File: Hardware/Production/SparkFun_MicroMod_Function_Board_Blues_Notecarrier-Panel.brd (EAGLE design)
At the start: 133.6 x 79.2 mm, 267 parts, among them J10 MICROMOD_FUNCTION_STANDARD, J14 NOTECARD, J15 MICROMOD_FUNCTION_STANDARD, J2 MICROMOD_FUNCTION_STANDARD, J6 NOTECARD, J9 NOTECARD, Q1 220mA/50V/3.5Ω, Q10 220mA/50V/3.5Ω, Q11 20V/4.2A/52mΩ/1.4W, Q12 20V/4.2A/52mΩ/1.4W, Q2 20V/4.2A/52mΩ/1.4W, Q3 220mA/50V/3.5Ω, Q4 20V/4.2A/52mΩ/1.4W, Q5 220mA/50V/3.5Ω, Q6 220mA/50V/3.5Ω, Q7 20V/4.2A/52mΩ/1.4W, Q8 20V/4.2A/52mΩ/1.4W, Q9 220mA/50V/3.5Ω, U1 EEPROM, U2 TCR2EF33, U3 EEPROM, U4 TCR2EF33, U5 EEPROM, U6 TCR2EF33

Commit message: Added v02 panel/gerbers.
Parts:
- removed ANT_PWR2, WP2: JUMPER-SMT_2_NO_SILK, SparkFun-Jumpers:SMT-JUMPER_2_NO_SILK
- removed AUX_EN_LED2, PWR_LED2, SHLD2, VIO_LED2: JUMPER-SMT_2_NC_TRACE_SILK, SparkFun-Jumpers:SMT-JUMPER_2_NC_TRACE_SILK
- removed C21, C23: 0.1uF, SparkFun-Capacitors:0402-TIGHT
- removed C22: 10uF, SparkFun-Capacitors:0805
- removed C24: 1.0uF, SparkFun-Capacitors:0402-TIGHT
- removed D21: RED, SparkFun-LED:LED-0603
- removed D22: BLUE, SparkFun-LED:LED-0603
- removed D23, D24: 0.5A/40V/420mV, SparkFun-DiscreteSemi:SOD-323
- removed FD10, FD11, FD12, FD9: FIDUCIALUFIDUCIAL, SparkFun-Aesthetics:FIDUCIAL-MICRO
- removed H3: STAND-OFF-REFLOW-M2.5_2.5MM_TALL, SparkFun-Hardware:STAND-OFF-REFLOW-M2.5
- removed J11: (no value), SparkFun-Connectors:USB-C-16P-2LAYER-PADS
- removed J12: (no value), SparkFun-Connectors:NANO_SIM_MOLEX_104224-0820
- removed J13: (no value), SparkFun-Connectors:1X06_NO_SILK
- removed J14: NOTECARD, SparkFun_MicroMod_Function_Board_Blues_Notecarrier:M.2-CONNECTOR-E
- removed J15: MICROMOD_FUNCTION_STANDARD, SparkFun-MicroMod:M.2-CARD-E-22_FUNCTION_STANDARD
- removed LOGO5: OSHW-LOGOMINI, SparkFun-Aesthetics:OSHW-LOGO-MINI
- removed LOGO6: SFE_LOGO_NAME_FLAME.1_INCH, SparkFun-Aesthetics:SFE_LOGO_NAME_FLAME_.1
- removed MEAS2: JUMPER-COMBO_2_NC_TRACE, SparkFun-Jumpers:COMBO-JUMPER_2_NC_TRACE
- removed R35, R36, R37, R44, R45: 10k, SparkFun-Resistors:0402-TIGHT
- removed R38, R39: 5.1k, SparkFun-Resistors:0402-TIGHT
- removed R40, R41: 1k, SparkFun-Resistors:0402-TIGHT
- removed R42: 4.7k, SparkFun-Resistors:0402-TIGHT
- removed R43: 2.2M, SparkFun-Resistors:0402-TIGHT
- removed R46, R47: 100, SparkFun-Resistors:0402-TIGHT
- removed R48: 1, SparkFun-Resistors:0603
- removed S3: MOMENTARY-SWITCH-SPST-SMD-4.6X2.8MM, SparkFun-Switches:TACTILE_SWITCH_SMD_4.6X2.8MM
- removed U$55, U$84: (no value), SparkFun-MicroMod:MICROMOD_LOGO_.3
- removed U$56, U$85: (no value), SparkFun-MicroMod:MICROMOD_MI_LOGO_.35
- removed U$57, U$86: (no value), output:#_AUX1#MCU_#DFU_STAT##0
- removed U$58, U$87: (no value), output:#AUX_EN_#0
- removed U$59: (no value), output:AEN1
- removed U$60: (no value), output:VIN3
- removed U$61: (no value), output:VIO4
- removed U$62: (no value), output:##RESET##9
- removed U$63: (no value), SparkFun-Aesthetics:SFE_LOGO_FLAME_STOP_.1
- removed U$64: (no value), output:#_GND_#0
- removed U$65: (no value), output:#_AUX4#MCU_#RST##0
- removed U$66: (no value), output:#_AUX3#MCU_#BOOT##0
- removed U$67: (no value), output:#_AUX2#0
- removed U$68: (no value), output:#_AUX_EN#0
- removed U$69: (no value), SparkFun-Aesthetics:SFE_LOGO_NAME_FLAME_.1
- removed U$70: (no value), output:BLUES_WIRELESS_NOTECARRIER1
- removed U$71: (no value), output:#_WP#2
- removed U$72, U$73: (no value), output:#MEAS#4
- removed U$74: (no value), output:#_ANT_PWR#5
- removed U$75: (no value), output:#PWR_LED_#17
- removed U$76: (no value), output:#AUX_EN_LED_#20
- removed U$77: (no value), output:#VIO_LED_#21
- removed U$78: (no value), output:#_SHLD#23
- removed U$79: (no value), output:#_GND_#24
- removed U$80: (no value), output:#AUX4#MCU_#RST##0
- removed U$81: (no value), output:#AUX3#MCU_#BOOT##0
- removed U$82: (no value), output:#AUX2_#0
- removed U$83: (no value), output:#AUX1#MCU_#DFU_STAT##0
- removed U5: EEPROM, SparkFun-IC-Memory:SO08
- removed U6: TCR2EF33, SparkFun_MicroMod_Function_Board_Blues_Notecarrier:SOT23-5
- added RGB, RGB1: JUMPER-SMT_2_NC_TRACE_SILK, SparkFun-Jumpers:SMT-JUMPER_2_NC_TRACE_SILK
- C10, C11: value 100uF -> 0.1uF; device SparkFun-Capacitors:PANASONIC_D -> SparkFun-Capacitors:0402-TIGHT
- C12, C13: value 0.1uF -> 100uF; device SparkFun-Capacitors:0402-TIGHT -> SparkFun-Capacitors:PANASONIC_D
- C14: value 10uF -> 0.1uF; device SparkFun-Capacitors:0805 -> SparkFun-Capacitors:0402-TIGHT
- C16: value 1.0uF -> 10uF; device SparkFun-Capacitors:0402-TIGHT -> SparkFun-Capacitors:0805
- C18, C19: value 100uF -> 1.0uF; device SparkFun-Capacitors:PANASONIC_D -> SparkFun-Capacitors:0402-TIGHT
- C9: value 0.1uF -> 1.0uF
- D10: value 3A/10V/280mV -> WS2812_2020; device SparkFun-DiscreteSemi:SOD-323 -> SparkFun-LED:WS2812-2020
- D11: value 3A/10V/280mV -> PRTR5V0U2F; device SparkFun-DiscreteSemi:SOD-323 -> SparkFun-IC-Power:SOT886
- D12, D13: value RED -> 3A/10V/280mV; device SparkFun-LED:LED-0603 -> SparkFun-DiscreteSemi:SOD-323
- D14: value BLUE -> RED
- D15: value 0.5A/40V/420mV -> RED; device SparkFun-DiscreteSemi:SOD-323 -> SparkFun-LED:LED-0603
- D16: value 0.5A/40V/420mV -> BLUE; device SparkFun-DiscreteSemi:SOD-323 -> SparkFun-LED:LED-0603
- D17: value PRTR5V0U2F -> 0.5A/40V/420mV; device SparkFun-IC-Power:SOT886 -> SparkFun-DiscreteSemi:SOD-323
- D18: value 3A/10V/280mV -> 0.5A/40V/420mV
- D19: value 3A/10V/280mV -> SMBJP6KE6.8A-TP; device SparkFun-DiscreteSemi:SOD-323 -> SparkFun_MicroMod_Function_Board_Blues_Notecarrier:DO-214AA
- D20: value RED -> WS2812_2020; device SparkFun-LED:LED-0603 -> SparkFun-LED:WS2812-2020
- D9: value PRTR5V0U2F -> SMBJP6KE6.8A-TP; device SparkFun-IC-Power:SOT886 -> SparkFun_MicroMod_Function_Board_Blues_Notecarrier:DO-214AA
- J10: value MICROMOD_FUNCTION_STANDARD -> (none); device SparkFun-MicroMod:M.2-CARD-E-22_FUNCTION_STANDARD -> SparkFun-Connectors:1X04_NO_SILK
- J3: device SparkFun-Connectors:USB-C-16P-2LAYER-PADS -> SparkFun-Connectors:1X04_NO_SILK
- J4: device SparkFun-Connectors:1X06_NO_SILK -> SparkFun-Connectors:USB-C-16P-2LAYER-PADS
- J8: value (none) -> NOTECARD; device SparkFun-Connectors:1X06_NO_SILK -> SparkFun_MicroMod_Function_Board_Blues_Notecarrier:M.2-CONNECTOR-E
- J9: value NOTECARD -> MICROMOD_FUNCTION_STANDARD; device SparkFun_MicroMod_Function_Board_Blues_Notecarrier:M.2-CONNECTOR-E -> SparkFun-MicroMod:M.2-CARD-E-22_FUNCTION_STANDARD
- Q10, Q6, Q9: value 220mA/50V/3.5Ω -> 20V/4.2A/52mΩ/1.4W
- Q11, Q7, Q8: value 20V/4.2A/52mΩ/1.4W -> 220mA/50V/3.5Ω
- R17: value 10k -> 100
- R18: value 560Ω -> 10k
- R19: value 10k -> 560Ω
- R22: value 5.1k -> 10k
- R24: value 1k -> 5.1k
- R26: value 4.7k -> 1k
- R27: value 2.2M -> 2.2k
- R28: value 10k -> 2.2M
- R34: value 560Ω -> 100
- R6: value 4.7k -> 2.2k
- U$10: device output:#_AUX3#MCU_#BOOT##0 -> notehub:NOTEHUB_BLUES#SVG7
- U$11: device output:#_AUX2#0 -> output:#_ATXO#0
- U$12: device output:#_AUX1#MCU_#DFU_STAT##0 -> output:#AUX_TX_#0
- U$13: device output:#_AUX_EN#0 -> output:#_AEN#0
- U$14: device SparkFun-Aesthetics:SFE_LOGO_NAME_FLAME_.1 -> SparkFun-Aesthetics:SFE_LOGO_NAME_FLAME_.2
- U$15: device output:BLUES_WIRELESS_NOTECARRIER1 -> output:#AUX_RX_#0
- U$23: device output:AEN1 -> notehub:NOTEHUB_BLUES#SVG5
- U$24: device output:#AUX4#MCU_#RST##0 -> output:#RGB_#0
- U$25: device output:#AUX3#MCU_#BOOT##0 -> output:AEN1
- U$26: device output:#AUX2_#0 -> output:VIN3
- U$27: device output:#AUX1#MCU_#DFU_STAT##0 -> output:VIO4
- U$28: device SparkFun-MicroMod:MICROMOD_LOGO_.3 -> SparkFun-Aesthetics:SFE_LOGO_FLAME_STOP_.1
- U$31: device output:VIN3 -> SparkFun-MicroMod:MICROMOD_LOGO_.5
- U$32: device output:VIO4 -> output:#_GND_#0
- U$33: device output:##RESET##9 -> SparkFun-Aesthetics:SFE_LOGO_NAME_FLAME_.2
- U$34: device SparkFun-Aesthetics:SFE_LOGO_FLAME_STOP_.1 -> output:#_WP#2
- U$35: device output:#_GND_#0 -> output:#MEAS#4
- U$36: device output:#_AUX4#MCU_#RST##0 -> output:#MEAS#4
- U$37: device output:#_AUX3#MCU_#BOOT##0 -> output:#_ANT_PWR#5
- U$38: device output:#_AUX2#0 -> output:#PWR_LED_#17
- U$39: device output:#_AUX_EN#0 -> output:#AUX_EN_LED_#20
- U$40: device SparkFun-Aesthetics:SFE_LOGO_NAME_FLAME_.1 -> output:#VIO_LED_#21
- U$41: device output:BLUES_WIRELESS_NOTECARRIER1 -> output:#_SHLD#23
- U$42: device output:#_WP#2 -> output:#_GND_#24
- U$43: device output:#MEAS#4 -> SparkFun-MicroMod:MICROMOD_MI_LOGO_.35
- U$44: device output:#MEAS#4 -> output:#AUX_EN_#0
- U$45: device output:#_ANT_PWR#5 -> notehub:NOTEHUB_BLUES#SVG5
- U$46: device output:#PWR_LED_#17 -> SparkFun-MicroMod:MICROMOD_LOGO_.5
- U$47: device output:#AUX_EN_LED_#20 -> output:BLUES_WIRELESS_NOTECARRIER0
- U$48: device output:#VIO_LED_#21 -> notehub:NOTEHUB_BLUES#SVG7
- U$49: device output:#_SHLD#23 -> output:#AUX_TX_#0
- U$5: device output:##RESET##9 -> output:#_ARXI#0
- U$50: device output:#_GND_#24 -> output:#AUX_RX_#0
- U$51: device output:#AUX4#MCU_#RST##0 -> output:#_ARXI#0
- U$52: device output:#AUX3#MCU_#BOOT##0 -> output:#_ATXO#0
- U$53: device output:#AUX2_#0 -> output:#_AEN#0
- U$54: device output:#AUX1#MCU_#DFU_STAT##0 -> output:#RGB_#0
- U$9: device output:#_AUX4#MCU_#RST##0 -> output:BLUES_WIRELESS_NOTECARRIER0
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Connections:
- removed net !RESET!: J6.67, S1.3, S1.4
- removed net !RESET!1: J9.67, S2.3, S2.4
- removed net !RESET!2: J14.67, S3.3, S3.4
- removed net 3.3V2: C17.1, C20.1, D20.A, D23.C, D24.C, J14.2, J14.4, R33.1, R44.1, U5.8
- removed net 3V3_IN2: J15.73, Q11.2, R35.1, R36.2
- removed net A6: J15.36, U5.1
- removed net A7: J15.32, U5.3
- removed net A8: J15.34, U5.2
- removed net ATTN2: J14.54, J15.53
- removed net AUX1: J10.57, J8.5, J9.48
- removed net AUX1/MCU_!DFU_STAT!: J2.10, J4.6, J6.46
- removed net AUX1/MCU_!DFU_STAT!1: J10.10, J8.6, J9.46
- removed net AUX1/MCU_!DFU_STAT!2: J13.6, J14.46, J15.10
- removed net AUX2: J2.57, J4.5, J6.48
- removed net AUX3: J13.5, J14.48, J15.57
- removed net AUX3/MCU_!BOOT!: J2.66, J4.4, J6.50
- removed net AUX3/MCU_!BOOT!1: J10.66, J8.4, J9.50
- removed net AUX3/MCU_!BOOT!2: J13.4, J14.50, J15.66
- removed net AUX4/MCU_!RST!: J2.68, J4.3, J6.52
- removed net AUX4/MCU_!RST!1: J10.68, J8.3, J9.52
- removed net AUX4/MCU_!RST!2: J13.3, J14.52, J15.68
- removed net AUX_EN2: D22.A, J13.2, J14.56, J15.55, R44.2
- removed net AUX_RX/MCU_TX2: J14.58, J15.4
- removed net AUX_TX/MCU_RX2: J14.60, J15.6
- removed net EWP2: J15.40, R33.2, U5.7, WP2.2
- removed net GND2: AUX_EN_LED2.1, C17.2, C18.-, C19.-, C20.2, C21.2, C22.2, C23.2, C24.2, D17.2, H3.1, J11.GND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
- removed net N$33 (its old number): Q5.3, R30.1
- removed net N$39 (its old number): Q12.1, R37.1, R47.2
- removed net N$43: D20.C, R40.2
- removed net N$44: D21.C, R41.2
- removed net N$45: PWR_LED2.2, R41.1
- removed net N$46: R40.1, VIO_LED2.2
- removed net N$47: D22.C, R42.2
- removed net N$48: AUX_EN_LED2.2, R42.1
- removed net N$49: R45.1, U6.3
- removed net N$50: C24.1, D23.A, U6.5
- removed net N$51: D24.A, Q11.3
- removed net N$52: Q9.3, R46.1
- removed net N$53: Q10.3, R47.1
- removed net N$54: MEAS2.2, MEAS2.4, R48.1
- removed net NOTECARD_RX2: J14.62, J15.13
- removed net NOTECARD_TX2: J14.64, J15.15
- removed net PWR_EN2: Q10.1, Q9.1, R34.1, R35.2
- removed net SCL2: J14.40, J15.21, U5.6
- removed net SDA2: J14.42, J15.19, U5.5
- removed net SHLD2: J11.SHLD1, J11.SHLD2, J11.SHLD3, J11.SHLD4, SHLD2.2
- removed net SIM_CLK2: J12.S3, J14.14
- removed net SIM_IO2: J12.S6, J14.12
- removed net SIM_RST2: J12.S2, J14.10
- removed net SIM_VCC2: C22.1, J12.S1, J14.8
- removed net USB_IN_N2: D17.3, J11.A7, J11.B7
- removed net USB_IN_P2: D17.1, J11.A6, J11.B6
- removed net USB_N2: D17.4, J14.9
- removed net USB_P2: D17.6, J14.7
- removed net VACT_GPS_IN2: ANT_PWR2.2, J14.22
- removed net VACT_GPS_OUT2: ANT_PWR2.1, J14.20
- removed net VCC2: D19.A, Q12.3
- removed net VCC_IN2: J15.72, J15.74, Q12.2, R37.2
- removed net VIN2: C18.+, C19.+, C21.1, C23.1, D21.A, J14.70, J14.72, J14.74, R43.2, R45.2, R48.2, U6.1
- removed net V_USB2: D17.5, D18.A, J11.VBUS1, J11.VBUS2, J14.13
- new net AUX1/DFU_!ACTIVE!/USR_BTN: C9.1, D9.C, J2.10, J6.46, S1.3, S1.4
- new net AUX1/DFU_!ACTIVE!/USR_BTN1: C19.1, D19.C, J8.46, J9.10, S2.3, S2.4
- new net AUX2/RGB: D10.DI, J2.57, J6.48
- new net AUX2/RGB1: D20.DI, J8.48, J9.57
- new net AUX3/DFU_!BOOT!: J2.66, J6.50
- new net AUX3/DFU_!BOOT!1: J8.50, J9.66
- new net AUX4/DFU_!RST!: J2.68, J6.52
- new net AUX4/DFU_!RST!1: J8.52, J9.68
- new net AUX_PWR: J2.55, Q5.1
- new net AUX_PWR1: J9.55, Q11.1
- new net N$30: R25.1, VIO_LED1.2
- new net N$35: D18.A, Q9.3
- net 3.3V: now also Q6.2, R10.2, RGB.2; no longer R10.1
- net 3.3V1: now also C11.1, C14.1, D14.A, D17.C, D18.C, J8.2, J8.4, Q12.2, R18.1, R33.2, RGB1.2; no longer C12.1, C9.1, D12.A, D15.C, D16.C, J9.2, J9.4, R17.1, R28.1
- net 3V3_IN1: now also J9.73, Q9.2, R20.1, R21.2; no longer J10.73, Q7.2, R19.1, R20.2
- net A3: now also J9.36; no longer J10.36
- net A4: now also J9.32; no longer J10.32
- net A5: now also J9.34; no longer J10.34
- net ATTN1: now also J8.54, J9.53; no longer J10.53, J9.54
- net AUX_EN: now also J3.4, Q6.3; no longer J2.55, J4.2, R10.2
- net AUX_EN1: now also D16.A, J10.4, J8.56, Q12.3; no longer D14.A, J10.55, J8.2, J9.56, R28.2
- net AUX_RX/MCU_TX: now also J2.6, J3.3; no longer J2.4
- net AUX_RX/MCU_TX1: now also J10.3, J8.58, J9.6; no longer J10.4, J9.58
- net AUX_TX/MCU_RX: now also J2.4, J3.2; no longer J2.6
- net AUX_TX/MCU_RX1: now also J10.2, J8.60, J9.4; no longer J10.6, J9.60
- net EWP1: now also J9.40, R18.2; no longer J10.40, R17.2
- net GND: now also C10.2, C9.2, D10.GND, D9.A, J3.1, Q5.2; no longer J4.1
- net GND1: now also C11.2, C12.-, C13.-, C17.2, C18.2, C19.2, C20.2, D11.2, D19.A, D20.GND, J4.GND, J4.GND2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; no longer C10.-, C11.-, C12.2, C13.2, C9.2, D9.2, J10.2, J10.33, J10.39, J10.45, J10.75, J10.8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
- net N$18: now also C10.1, D10.VCC, RGB.1; no longer J10.71, R18.2
- net N$19: now also Q6.1, R10.1, R17.2; no longer Q7.1, R20.1, R30.2
- net N$20: now also Q5.3, R17.1; no longer Q8.1, R21.1, R31.2
- net N$21: now also J9.71, R19.2; no longer J3.B5, R22.2
- net N$22: now also Q9.1, R21.1, R30.2; no longer J3.A5, R23.2
- net N$23: now also Q10.1, R22.1, R31.2; no longer D10.C, D11.C, MEAS1.1, MEAS1.3
- net N$24: now also J4.B5, R23.2; no longer D12.C, R24.2
- net N$25: now also J4.A5, R24.2; no longer D13.C, R25.2
- net N$26: now also D12.C, D13.C, MEAS1.1, MEAS1.3; no longer PWR_LED1.2, R25.1
- net N$27: now also D14.C, R25.2; no longer R24.1, VIO_LED1.2
- net N$28: now also D15.C; no longer D14.C
- net N$29: now also PWR_LED1.2; no longer AUX_EN_LED1.2
- net N$31: now also D16.C, R27.2; no longer C16.1, D15.A, U4.5
- net N$32: now also AUX_EN_LED1.2, R27.1; no longer D16.A, Q7.3
- net N$34: now also C18.1, D17.A, U4.5; no longer Q6.3, R31.1
- net N$36: now also Q7.3, R30.1; no longer J15.71, R34.2
- net N$38: now also Q8.3, R31.1; no longer Q11.1, R36.1, R46.2
- net N$40: now also C20.1, D20.VCC, RGB1.1; no longer J11.B5, R38.2
- net N$41: now also Q12.1, R33.1, R34.2; no longer J11.A5, R39.2
- net N$42: now also Q11.3, R34.1; no longer D18.C, D19.C, MEAS2.1, MEAS2.3
- net NOTECARD_RX1: now also J8.62, J9.13; no longer J10.13, J9.62
- net NOTECARD_TX1: now also J8.64, J9.15; no longer J10.15, J9.64
- net PWR_EN1: now also Q7.1, Q8.1, R19.1, R20.2; no longer Q5.1, Q6.1, R18.1, R19.2
- net SCL1: now also J8.40, J9.21; no longer J10.21, J9.40
- net SDA1: now also J8.42, J9.19; no longer J10.19, J9.42
- net SHLD1: now also J4.SHLD1, J4.SHLD2, J4.SHLD3, J4.SHLD4; no longer J3.SHLD1, J3.SHLD2, J3.SHLD3, J3.SHLD4
- net SIM_CLK1: now also J8.14; no longer J9.14
- net SIM_IO1: now also J8.12; no longer J9.12
- net SIM_RST1: now also J8.10; no longer J9.10
- net SIM_VCC1: now also C16.1, J8.8; no longer C14.1, J9.8
- net USB_IN_N1: now also D11.3, J4.A7, J4.B7; no longer D9.3, J3.A7, J3.B7
- net USB_IN_P1: now also D11.1, J4.A6, J4.B6; no longer D9.1, J3.A6, J3.B6
- net USB_N1: now also D11.4, J8.9; no longer D9.4, J9.9
- net USB_P1: now also D11.6, J8.7; no longer D9.6, J9.7
- net VACT_GPS_IN1: now also J8.22; no longer J9.22
- net VACT_GPS_OUT1: now also J8.20; no longer J9.20
- net VCC1: now also D13.A, Q10.3; no longer D11.A, Q8.3
- net VCC_IN1: now also J9.72, J9.74, Q10.2, R22.2; no longer J10.72, J10.74, Q8.2, R21.2
- net VIN1: now also C12.+, C13.+, C17.1, D15.A, J8.70, J8.72, J8.74, R28.2; no longer C10.+, C11.+, C13.1, D13.A, J9.70, J9.72, J9.74, R27.2
- net V_USB1: now also D11.5, D12.A, J4.VBUS1, J4.VBUS2, J8.13; no longer D10.A, D9.5, J3.VBUS1, J3.VBUS2, J9.13
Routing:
- net AUX_EN2: track 97.9 -> 0.00 mm, vias 7 -> 0
- net VIN2: track 92.7 -> 0.00 mm, vias 3 -> 0
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- added copper zone on layer 1, net AUX1/DFU_!ACTIVE!/USR_BTN
- added copper zone on layer 1, net AUX1/DFU_!ACTIVE!/USR_BTN1
- added copper zone on layer 1, net N$34
- removed copper zone on layer 1, net 3.3V2
- removed copper zone on layer 1, net GND2
- removed copper zone on layer 16, net GND2
- removed copper zone on layer 1, net N$31
- removed copper zone on layer 1, net N$50
- removed copper zone on layer 1, net SHLD2
- removed copper zone on layer 16, net SHLD2
- removed copper zone on layer 1, net SIM_VCC2
- removed copper zone on layer 16, net SIM_VCC2
- removed copper zone on layer 1, net VCC_IN2
- removed copper zone on layer 16, net VCC_IN2
- removed copper zone on layer 1, net VIN2
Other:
- board size 133.6 x 79.2 mm -> 95.6 x 79.2 mm
- board text added: "v02"
- board text removed: "v01"

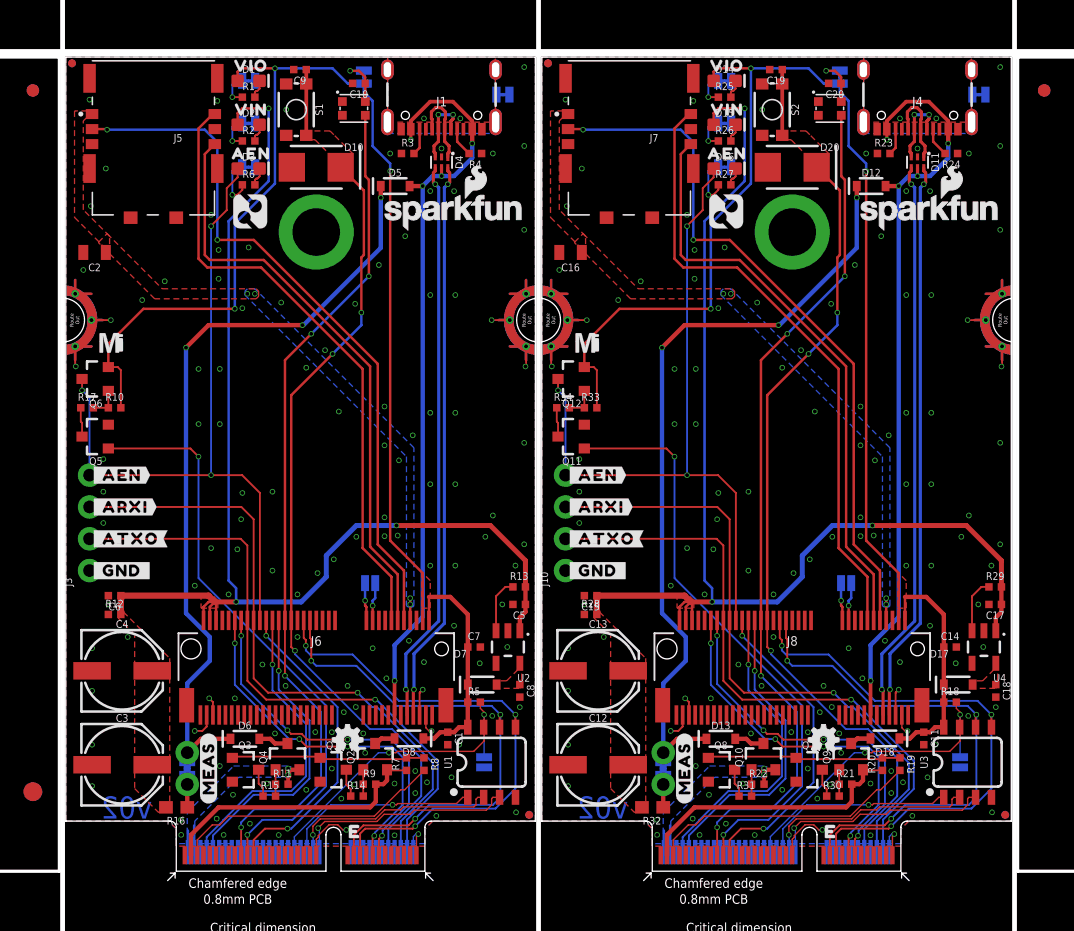
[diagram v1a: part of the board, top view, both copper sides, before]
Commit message: Swap Notecard RX/TX, add missing silk, add diode PROD-ID.
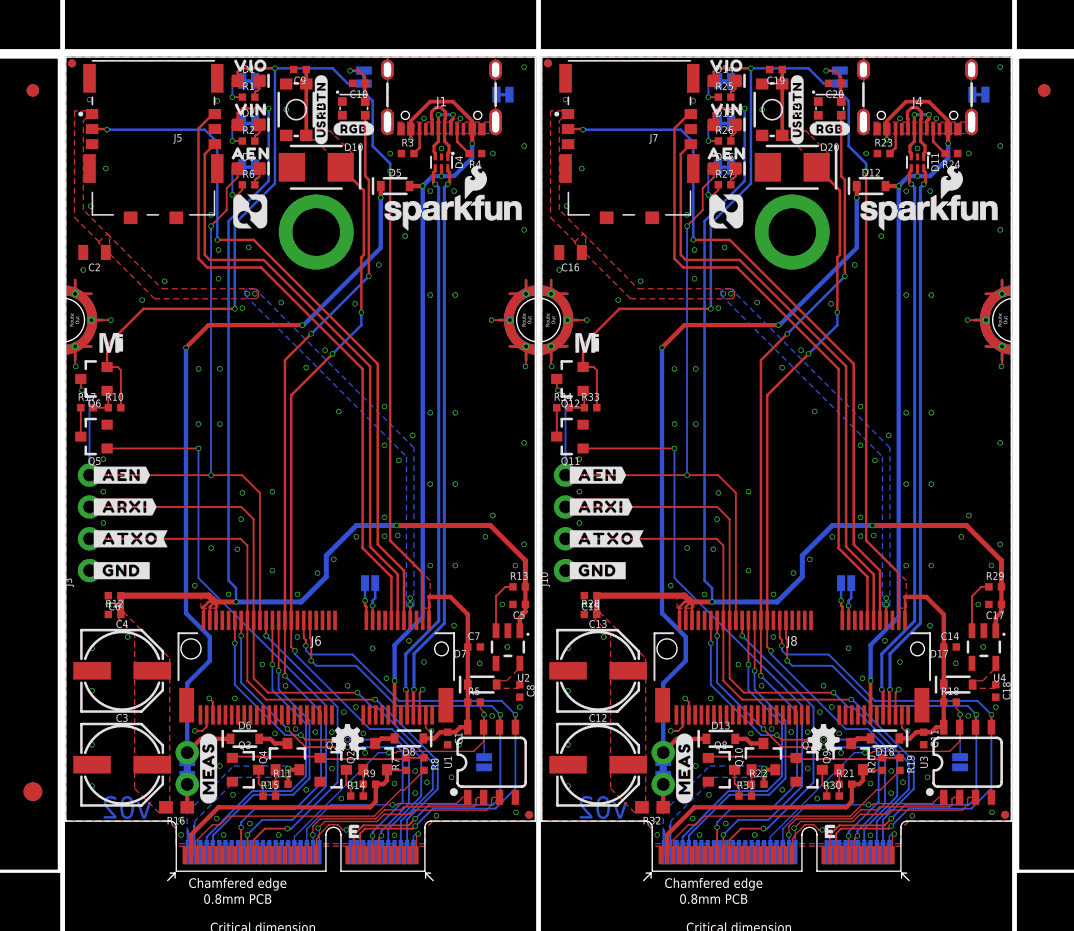
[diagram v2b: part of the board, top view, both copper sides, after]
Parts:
- added U$55: (no value), output:#_AEN#0
- added U$56: (no value), output:#RGB_#0
- added U$57: (no value), output:#USRBTN#0
- added U$58: (no value), output:#RGB#0
- U$25: device output:AEN1 -> output:#USRBTN#0
- U$26: device output:VIN3 -> output:#RGB#0
- U$27: device output:VIO4 -> output:AEN1
- U$28: device SparkFun-Aesthetics:SFE_LOGO_FLAME_STOP_.1 -> output:VIN3
- U$32: device output:#_GND_#0 -> output:VIO4
- U$33: device SparkFun-Aesthetics:SFE_LOGO_NAME_FLAME_.2 -> SparkFun-Aesthetics:SFE_LOGO_FLAME_STOP_.1
- U$34: device output:#_WP#2 -> output:#_GND_#0
- U$35: device output:#MEAS#4 -> SparkFun-Aesthetics:SFE_LOGO_NAME_FLAME_.2
- U$36: device output:#MEAS#4 -> output:#_WP#2
- U$37: device output:#_ANT_PWR#5 -> output:#MEAS#4
- U$38: device output:#PWR_LED_#17 -> output:#MEAS#4
- U$39: device output:#AUX_EN_LED_#20 -> output:#_ANT_PWR#5
- U$40: device output:#VIO_LED_#21 -> output:#PWR_LED_#17
- U$41: device output:#_SHLD#23 -> output:#AUX_EN_LED_#20
- U$42: device output:#_GND_#24 -> output:#VIO_LED_#21
- U$43: device SparkFun-MicroMod:MICROMOD_MI_LOGO_.35 -> output:#_SHLD#23
- U$44: device output:#AUX_EN_#0 -> output:#_GND_#24
- U$45: device notehub:NOTEHUB_BLUES#SVG5 -> SparkFun-MicroMod:MICROMOD_MI_LOGO_.35
- U$46: device SparkFun-MicroMod:MICROMOD_LOGO_.5 -> output:#AUX_EN_#0
- U$47: device output:BLUES_WIRELESS_NOTECARRIER0 -> notehub:NOTEHUB_BLUES#SVG5
- U$48: device notehub:NOTEHUB_BLUES#SVG7 -> SparkFun-MicroMod:MICROMOD_LOGO_.5
- U$49: device output:#AUX_TX_#0 -> output:BLUES_WIRELESS_NOTECARRIER0
- U$50: device output:#AUX_RX_#0 -> notehub:NOTEHUB_BLUES#SVG7
- U$51: device output:#_ARXI#0 -> output:#AUX_TX_#0
- U$52: device output:#_ATXO#0 -> output:#AUX_RX_#0
- U$53: device output:#_AEN#0 -> output:#_ARXI#0
- U$54: device output:#RGB_#0 -> output:#_ATXO#0
- moved U$38 52.7 mm to (49.4, 8.20), flipped to the top, turned to 90 degrees
- moved U$32 42.3 mm to (52.8, 64.3)
- moved U$42 41.8 mm to (59.9, 63.1)
- moved U$54 39.2 mm to (39.9, 26.5), flipped to the top, turned to 0 degrees
- moved U$35 36.4 mm to (56.8, 43.0), turned to 0 degrees
- moved U$43 36.3 mm to (72.0, 62.0), flipped to the bottom
- moved U$34 34.4 mm to (39.9, 24.0), flipped to the top
- moved U$39 33.8 mm to (56.7, 23.0)
- moved U$25 32.6 mm to (20.4, 60.8), turned to 90 degrees
- moved U$26 29.8 mm to (23.0, 59.2)
- moved U$36 21.3 mm to (70.7, 8.70), flipped to the bottom, turned to 0 degrees
- moved U$37 18.3 mm to (46.0, 8.20), turned to 90 degrees
- moved U$28 18.2 mm to (52.8, 60.8)
- moved U$47 17.2 mm to (51.4, 54.0), flipped to the top
- moved U$33 15.5 mm to (41.6, 46.5), flipped to the top
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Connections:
- net NOTECARD_RX: now also J2.15; no longer J2.13
- net NOTECARD_RX1: now also J9.15; no longer J9.13
- net NOTECARD_TX: now also J2.13; no longer J2.15
- net NOTECARD_TX1: now also J9.13; no longer J9.15
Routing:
- net NOTECARD_TX: track 29.8 -> 30.5 mm
- net NOTECARD_TX1: track 29.8 -> 30.5 mm
- net GND1: vias 127 -> 128
- net GND: vias 127 -> 128

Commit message: Rev to v10. Update RGB Silk. Repanelize for changes.
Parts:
- added ANT_PWR2, ANT_PWR3, ANT_PWR4, ANT_PWR5, WP2, WP3, WP4, WP5: JUMPER-SMT_2_NO_SILK, SparkFun-Jumpers:SMT-JUMPER_2_NO_SILK
- added AUX_EN_LED2, AUX_EN_LED3, AUX_EN_LED4, AUX_EN_LED5, PWR_LED2, PWR_LED3, PWR_LED4, PWR_LED5, RGB2, RGB3, RGB4, RGB5, SHLD2, SHLD3, SHLD4, SHLD5, VIO_LED2, VIO_LED3, VIO_LED4, VIO_LED5: JUMPER-SMT_2_NC_TRACE_SILK, SparkFun-Jumpers:SMT-JUMPER_2_NC_TRACE_SILK
- added C21, C24, C25, C27, C30, C31, C34, C35, C37, C40, C41, C44, C45, C47, C50, C51, C54, C55, C57, C60: 0.1uF, SparkFun-Capacitors:0402-TIGHT
- added C22, C23, C32, C33, C42, C43, C52, C53: 100uF, SparkFun-Capacitors:PANASONIC_D
- added C26, C36, C46, C56: 10uF, SparkFun-Capacitors:0805
- added C28, C29, C38, C39, C48, C49, C58, C59: 1.0uF, SparkFun-Capacitors:0402-TIGHT
- added D21, D31, D41, D51: PRTR5V0U2F, SparkFun-IC-Power:SOT886
- added D22, D23, D32, D33, D42, D43, D52, D53: 3A/10V/280mV, SparkFun-DiscreteSemi:SOD-323
- added D24, D25, D34, D35, D44, D45, D54, D55: RED, SparkFun-LED:LED-0603
- added D26, D36, D46, D56: BLUE, SparkFun-LED:LED-0603
- added D27, D28, D37, D38, D47, D48, D57, D58: 0.5A/40V/420mV, SparkFun-DiscreteSemi:SOD-323
- added D29, D39, D49, D59: SMBJP6KE6.8A-TP, SparkFun_MicroMod_Function_Board_Blues_Notecarrier:DO-214AA
- added D30, D40, D50, D60: WS2812_2020, SparkFun-LED:WS2812-2020
- added FD10, FD11, FD12, FD13, FD14, FD15, FD16, FD17, FD18, FD19, FD20, FD21, FD22, FD23, FD24, FD9: FIDUCIALUFIDUCIAL, SparkFun-Aesthetics:FIDUCIAL-MICRO
- added H3, H4, H5, H6: STAND-OFF-REFLOW-M2.5_2.5MM_TALL, SparkFun-Hardware:STAND-OFF-REFLOW-M2.5
- added J11, J16, J21, J26: (no value), SparkFun-Connectors:USB-C-16P-2LAYER-PADS
- added J12, J17, J22, J27: (no value), SparkFun-Connectors:NANO_SIM_MOLEX_104224-0820
- added J13, J18, J23, J28: NOTECARD, SparkFun_MicroMod_Function_Board_Blues_Notecarrier:M.2-CONNECTOR-E
- added J14, J19, J24, J29: MICROMOD_FUNCTION_STANDARD, SparkFun-MicroMod:M.2-CARD-E-22_FUNCTION_STANDARD
- added J15, J20, J25, J30: (no value), SparkFun-Connectors:1X04_NO_SILK
- added LOGO10, LOGO12, LOGO6, LOGO8: SFE_LOGO_NAME_FLAME.1_INCH, SparkFun-Aesthetics:SFE_LOGO_NAME_FLAME_.1
- added LOGO11, LOGO5, LOGO7, LOGO9: OSHW-LOGOMINI, SparkFun-Aesthetics:OSHW-LOGO-MINI
- added MEAS2, MEAS3, MEAS4, MEAS5: JUMPER-COMBO_2_NC_TRACE, SparkFun-Jumpers:COMBO-JUMPER_2_NC_TRACE
- added Q13, Q14, Q17, Q19, Q20, Q23, Q25, Q26, Q29, Q31, Q32, Q35: 220mA/50V/3.5Ω, SparkFun-DiscreteSemi:SOT23-3
- added Q15, Q16, Q18, Q21, Q22, Q24, Q27, Q28, Q30, Q33, Q34, Q36: 20V/4.2A/52mΩ/1.4W, SparkFun-DiscreteSemi:SOT23-3
- added R100, R49, R66, R83: 1, SparkFun-Resistors:0603
- added R101, R35, R37, R38, R39, R46, R50, R52, R54, R55, R56, R63, R67, R69, R71, R72, R73, R80, R84, R86, R88, R89, R90, R97: 10k, SparkFun-Resistors:0402-TIGHT
- added R102, R47, R48, R51, R64, R65, R68, R81, R82, R85, R98, R99: 100, SparkFun-Resistors:0402-TIGHT
- added R36, R53, R70, R87: 560Ω, SparkFun-Resistors:0402-TIGHT
- added R40, R41, R57, R58, R74, R75, R91, R92: 5.1k, SparkFun-Resistors:0402-TIGHT
- added R42, R43, R59, R60, R76, R77, R93, R94: 1k, SparkFun-Resistors:0402-TIGHT
- added R44, R61, R78, R95: 2.2k, SparkFun-Resistors:0402-TIGHT
- added R45, R62, R79, R96: 2.2M, SparkFun-Resistors:0402-TIGHT
- added S3, S4, S5, S6: MOMENTARY-SWITCH-SPST-SMD-4.6X2.8MM, SparkFun-Switches:TACTILE_SWITCH_SMD_4.6X2.8MM
- added U$100, U$129, U$158, U$71: (no value), output:#VIO_LED_#21
- added U$101, U$130, U$159, U$72: (no value), output:#_SHLD#23
- added U$102, U$131, U$160, U$73: (no value), output:#_GND_#24
- added U$103, U$132, U$161, U$74: (no value), SparkFun-MicroMod:MICROMOD_MI_LOGO_.35
- added U$104, U$133, U$162, U$75: (no value), output:#AUX_EN_#0
- added U$105, U$134, U$163, U$76: (no value), notehub:NOTEHUB_BLUES#SVG5
- added U$106, U$135, U$164, U$77: (no value), SparkFun-MicroMod:MICROMOD_LOGO_.5
- added U$107, U$136, U$165, U$78: (no value), output:BLUES_WIRELESS_NOTECARRIER0
- added U$108, U$137, U$166, U$79: (no value), notehub:NOTEHUB_BLUES#SVG7
- added U$109, U$138, U$167, U$80: (no value), output:#AUX_TX_#0
- added U$110, U$139, U$168, U$81: (no value), output:#AUX_RX_#0
- added U$111, U$140, U$169, U$82: (no value), output:#_ARXI#0
- added U$112, U$141, U$170, U$83: (no value), output:#_ATXO#0
- added U$113, U$142, U$171, U$84: (no value), output:#_AEN#0
- added U$114, U$143, U$172, U$85: (no value), output:#RGB_#0
- added U$115, U$144, U$173, U$86: (no value), output:#USRBTN#0
- added U$116, U$145, U$174, U$87: (no value), output:RGB0
- added U$117, U$146, U$59, U$88: (no value), output:AEN1
- added U$118, U$147, U$60, U$89: (no value), output:VIN3
- added U$119, U$148, U$61, U$90: (no value), output:VIO4
- added U$120, U$149, U$62, U$91: (no value), SparkFun-Aesthetics:SFE_LOGO_FLAME_STOP_.1
- added U$121, U$150, U$63, U$92: (no value), output:#_GND_#0
- added U$122, U$151, U$64, U$93: (no value), SparkFun-Aesthetics:SFE_LOGO_NAME_FLAME_.2
- added U$123, U$152, U$65, U$94: (no value), output:#_WP#2
- added U$124, U$125, U$153, U$154, U$66, U$67, U$95, U$96: (no value), output:#MEAS#4
- added U$126, U$155, U$68, U$97: (no value), output:#_ANT_PWR#5
- added U$127, U$156, U$69, U$98: (no value), output:#PWR_LED_#17
- added U$128, U$157, U$70, U$99: (no value), output:#AUX_EN_LED_#20
- added U10, U12, U6, U8: TCR2EF33, SparkFun_MicroMod_Function_Board_Blues_Notecarrier:SOT23-5
- added U11, U5, U7, U9: EEPROM, SparkFun-IC-Memory:SO08
- U$26, U$58: device output:#RGB#0 -> output:RGB0
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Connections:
- new net 3.3V2: C21.1, C24.1, D24.A, D27.C, D28.C, J13.2, J13.4, Q18.2, R35.1, R50.2, RGB2.2, U5.8
- new net 3.3V3: C31.1, C34.1, D34.A, D37.C, D38.C, J18.2, J18.4, Q24.2, R52.1, R67.2, RGB3.2, U7.8
- new net 3.3V4: C41.1, C44.1, D44.A, D47.C, D48.C, J23.2, J23.4, Q30.2, R69.1, R84.2, RGB4.2, U9.8
- new net 3.3V5: C51.1, C54.1, D54.A, D57.C, D58.C, J28.2, J28.4, Q36.2, R101.2, R86.1, RGB5.2, U11.8
- new net 3V3_IN2: J14.73, Q15.2, R37.1, R38.2
- new net 3V3_IN3: J19.73, Q21.2, R54.1, R55.2
- new net 3V3_IN4: J24.73, Q27.2, R71.1, R72.2
- new net 3V3_IN5: J29.73, Q33.2, R88.1, R89.2
- new net A10: J19.32, U7.3
- new net A11: J19.34, U7.2
- new net A12: J24.36, U9.1
- new net A13: J24.32, U9.3
- new net A14: J24.34, U9.2
- new net A15: J29.36, U11.1
- new net A16: J29.32, U11.3
- new net A17: J29.34, U11.2
- new net A6: J14.36, U5.1
- new net A7: J14.32, U5.3
- new net A8: J14.34, U5.2
- new net A9: J19.36, U7.1
- new net ATTN2: J13.54, J14.53
- new net ATTN3: J18.54, J19.53
- new net ATTN4: J23.54, J24.53
- new net ATTN5: J28.54, J29.53
- new net AUX1/DFU_!ACTIVE!/USR_BTN2: C29.1, D29.C, J13.46, J14.10, S3.3, S3.4
- new net AUX1/DFU_!ACTIVE!/USR_BTN3: C39.1, D39.C, J18.46, J19.10, S4.3, S4.4
- new net AUX1/DFU_!ACTIVE!/USR_BTN4: C49.1, D49.C, J23.46, J24.10, S5.3, S5.4
- new net AUX1/DFU_!ACTIVE!/USR_BTN5: C59.1, D59.C, J28.46, J29.10, S6.3, S6.4
- new net AUX2/RGB2: D30.DI, J13.48, J14.57
- new net AUX2/RGB3: D40.DI, J18.48, J19.57
- new net AUX2/RGB4: D50.DI, J23.48, J24.57
- new net AUX2/RGB5: D60.DI, J28.48, J29.57
- new net AUX3/DFU_!BOOT!2: J13.50, J14.66
- new net AUX3/DFU_!BOOT!3: J18.50, J19.66
- new net AUX3/DFU_!BOOT!4: J23.50, J24.66
- new net AUX3/DFU_!BOOT!5: J28.50, J29.66
- new net AUX4/DFU_!RST!2: J13.52, J14.68
- new net AUX4/DFU_!RST!3: J18.52, J19.68
- new net AUX4/DFU_!RST!4: J23.52, J24.68
- new net AUX4/DFU_!RST!5: J28.52, J29.68
- new net AUX_EN2: D26.A, J13.56, J15.4, Q18.3
- new net AUX_EN3: D36.A, J18.56, J20.4, Q24.3
- new net AUX_EN4: D46.A, J23.56, J25.4, Q30.3
- new net AUX_EN5: D56.A, J28.56, J30.4, Q36.3
- new net AUX_PWR2: J14.55, Q17.1
- new net AUX_PWR3: J19.55, Q23.1
- new net AUX_PWR4: J24.55, Q29.1
- new net AUX_PWR5: J29.55, Q35.1
- new net AUX_RX/MCU_TX2: J13.58, J14.6, J15.3
- new net AUX_RX/MCU_TX3: J18.58, J19.6, J20.3
- new net AUX_RX/MCU_TX4: J23.58, J24.6, J25.3
- new net AUX_RX/MCU_TX5: J28.58, J29.6, J30.3
- new net AUX_TX/MCU_RX2: J13.60, J14.4, J15.2
- new net AUX_TX/MCU_RX3: J18.60, J19.4, J20.2
- new net AUX_TX/MCU_RX4: J23.60, J24.4, J25.2
- new net AUX_TX/MCU_RX5: J28.60, J29.4, J30.2
- new net EWP2: J14.40, R35.2, U5.7, WP2.2
- new net EWP3: J19.40, R52.2, U7.7, WP3.2
- new net EWP4: J24.40, R69.2, U9.7, WP4.2
- new net EWP5: J29.40, R86.2, U11.7, WP5.2
- new net GND2: AUX_EN_LED2.1, C21.2, C22.-, C23.-, C24.2, C25.2, C26.2, C27.2, C28.2, C29.2, C30.2, D21.2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
- new net GND3: AUX_EN_LED3.1, C31.2, C32.-, C33.-, C34.2, C35.2, C36.2, C37.2, C38.2, C39.2, C40.2, D31.2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
- new net GND4: AUX_EN_LED4.1, C41.2, C42.-, C43.-, C44.2, C45.2, C46.2, C47.2, C48.2, C49.2, C50.2, D41.2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
- new net GND5: AUX_EN_LED5.1, C51.2, C52.-, C53.-, C54.2, C55.2, C56.2, C57.2, C58.2, C59.2, C60.2, D51.2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
- new net N$100: Q25.3, R81.1
- new net N$101: Q26.3, R82.1
- new net N$102: MEAS4.2, MEAS4.4, R83.1
- new net N$103: C50.1, D50.VCC, RGB4.1
- new net N$104: Q30.1, R84.1, R85.2
- new net N$105: Q29.3, R85.1
- new net N$106: J29.71, R87.2
- new net N$107: Q33.1, R89.1, R98.2
- new net N$108: Q34.1, R90.1, R99.2
- new net N$109: J26.B5, R91.2
- new net N$110: J26.A5, R92.2
- new net N$111: D52.C, D53.C, MEAS5.1, MEAS5.3
- new net N$112: D54.C, R93.2
- new net N$113: D55.C, R94.2
- new net N$114: PWR_LED5.2, R94.1
- new net N$115: R93.1, VIO_LED5.2
- new net N$116: D56.C, R95.2
- new net N$117: AUX_EN_LED5.2, R95.1
- new net N$118: R97.1, U12.3
- new net N$119: C58.1, D57.A, U12.5
- new net N$120: D58.A, Q33.3
- new net N$121: Q31.3, R98.1
- new net N$122: Q32.3, R99.1
- new net N$123: MEAS5.2, MEAS5.4, R100.1
- new net N$124: C60.1, D60.VCC, RGB5.1
- new net N$125: Q36.1, R101.1, R102.2
- new net N$126: Q35.3, R102.1
- new net N$43: J14.71, R36.2
- new net N$44: Q15.1, R38.1, R47.2
- new net N$45: Q16.1, R39.1, R48.2
- new net N$46: J11.B5, R40.2
- new net N$47: J11.A5, R41.2
- new net N$48: D22.C, D23.C, MEAS2.1, MEAS2.3
- new net N$49: D24.C, R42.2
- new net N$50: D25.C, R43.2
- new net N$51: PWR_LED2.2, R43.1
- new net N$52: R42.1, VIO_LED2.2
- new net N$53: D26.C, R44.2
- new net N$54: AUX_EN_LED2.2, R44.1
- new net N$55: R46.1, U6.3
- new net N$56: C28.1, D27.A, U6.5
- new net N$57: D28.A, Q15.3
- new net N$58: Q13.3, R47.1
- new net N$59: Q14.3, R48.1
- new net N$60: MEAS2.2, MEAS2.4, R49.1
- new net N$61: C30.1, D30.VCC, RGB2.1
- new net N$62: Q18.1, R50.1, R51.2
- new net N$63: Q17.3, R51.1
- new net N$64: J19.71, R53.2
- new net N$65: Q21.1, R55.1, R64.2
- new net N$66: Q22.1, R56.1, R65.2
- new net N$67: J16.B5, R57.2
- new net N$68: J16.A5, R58.2
- new net N$69: D32.C, D33.C, MEAS3.1, MEAS3.3
- new net N$70: D34.C, R59.2
- new net N$71: D35.C, R60.2
- new net N$72: PWR_LED3.2, R60.1
- new net N$73: R59.1, VIO_LED3.2
- new net N$74: D36.C, R61.2
- new net N$75: AUX_EN_LED3.2, R61.1
- new net N$76: R63.1, U8.3
- new net N$77: C38.1, D37.A, U8.5
- new net N$78: D38.A, Q21.3
- new net N$79: Q19.3, R64.1
- new net N$80: Q20.3, R65.1
- new net N$81: MEAS3.2, MEAS3.4, R66.1
- new net N$82: C40.1, D40.VCC, RGB3.1
- new net N$83: Q24.1, R67.1, R68.2
- new net N$84: Q23.3, R68.1
- new net N$85: J24.71, R70.2
- new net N$86: Q27.1, R72.1, R81.2
- new net N$87: Q28.1, R73.1, R82.2
- new net N$88: J21.B5, R74.2
- new net N$89: J21.A5, R75.2
- new net N$90: D42.C, D43.C, MEAS4.1, MEAS4.3
- new net N$91: D44.C, R76.2
- new net N$92: D45.C, R77.2
- new net N$93: PWR_LED4.2, R77.1
- new net N$94: R76.1, VIO_LED4.2
- new net N$95: D46.C, R78.2
- new net N$96: AUX_EN_LED4.2, R78.1
- new net N$97: R80.1, U10.3
- new net N$98: C48.1, D47.A, U10.5
- new net N$99: D48.A, Q27.3
- new net NOTECARD_RX2: J13.62, J14.15
- new net NOTECARD_RX3: J18.62, J19.15
- new net NOTECARD_RX4: J23.62, J24.15
- new net NOTECARD_RX5: J28.62, J29.15
- new net NOTECARD_TX2: J13.64, J14.13
- new net NOTECARD_TX3: J18.64, J19.13
- new net NOTECARD_TX4: J23.64, J24.13
- new net NOTECARD_TX5: J28.64, J29.13
- new net PWR_EN2: Q13.1, Q14.1, R36.1, R37.2
- new net PWR_EN3: Q19.1, Q20.1, R53.1, R54.2
- new net PWR_EN4: Q25.1, Q26.1, R70.1, R71.2
- new net PWR_EN5: Q31.1, Q32.1, R87.1, R88.2
- new net SCL2: J13.40, J14.21, U5.6
- new net SCL3: J18.40, J19.21, U7.6
- new net SCL4: J23.40, J24.21, U9.6
- new net SCL5: J28.40, J29.21, U11.6
- new net SDA2: J13.42, J14.19, U5.5
- new net SDA3: J18.42, J19.19, U7.5
- new net SDA4: J23.42, J24.19, U9.5
- new net SDA5: J28.42, J29.19, U11.5
- new net SHLD2: J11.SHLD1, J11.SHLD2, J11.SHLD3, J11.SHLD4, SHLD2.2
- new net SHLD3: J16.SHLD1, J16.SHLD2, J16.SHLD3, J16.SHLD4, SHLD3.2
- new net SHLD4: J21.SHLD1, J21.SHLD2, J21.SHLD3, J21.SHLD4, SHLD4.2
- new net SHLD5: J26.SHLD1, J26.SHLD2, J26.SHLD3, J26.SHLD4, SHLD5.2
- new net SIM_CLK2: J12.S3, J13.14
- new net SIM_CLK3: J17.S3, J18.14
- new net SIM_CLK4: J22.S3, J23.14
- new net SIM_CLK5: J27.S3, J28.14
- new net SIM_IO2: J12.S6, J13.12
- new net SIM_IO3: J17.S6, J18.12
- new net SIM_IO4: J22.S6, J23.12
- new net SIM_IO5: J27.S6, J28.12
- new net SIM_RST2: J12.S2, J13.10
- new net SIM_RST3: J17.S2, J18.10
- new net SIM_RST4: J22.S2, J23.10
- new net SIM_RST5: J27.S2, J28.10
- new net SIM_VCC2: C26.1, J12.S1, J13.8
- new net SIM_VCC3: C36.1, J17.S1, J18.8
- new net SIM_VCC4: C46.1, J22.S1, J23.8
- new net SIM_VCC5: C56.1, J27.S1, J28.8
- new net USB_IN_N2: D21.3, J11.A7, J11.B7
- new net USB_IN_N3: D31.3, J16.A7, J16.B7
- new net USB_IN_N4: D41.3, J21.A7, J21.B7
- new net USB_IN_N5: D51.3, J26.A7, J26.B7
- new net USB_IN_P2: D21.1, J11.A6, J11.B6
- new net USB_IN_P3: D31.1, J16.A6, J16.B6
- new net USB_IN_P4: D41.1, J21.A6, J21.B6
- new net USB_IN_P5: D51.1, J26.A6, J26.B6
- new net USB_N2: D21.4, J13.9
- new net USB_N3: D31.4, J18.9
- new net USB_N4: D41.4, J23.9
- new net USB_N5: D51.4, J28.9
- new net USB_P2: D21.6, J13.7
- new net USB_P3: D31.6, J18.7
- new net USB_P4: D41.6, J23.7
- new net USB_P5: D51.6, J28.7
- new net VACT_GPS_IN2: ANT_PWR2.2, J13.22
- new net VACT_GPS_IN3: ANT_PWR3.2, J18.22
- new net VACT_GPS_IN4: ANT_PWR4.2, J23.22
- new net VACT_GPS_IN5: ANT_PWR5.2, J28.22
- new net VACT_GPS_OUT2: ANT_PWR2.1, J13.20
- new net VACT_GPS_OUT3: ANT_PWR3.1, J18.20
- new net VACT_GPS_OUT4: ANT_PWR4.1, J23.20
- new net VACT_GPS_OUT5: ANT_PWR5.1, J28.20
- new net VCC2: D23.A, Q16.3
- new net VCC3: D33.A, Q22.3
- new net VCC4: D43.A, Q28.3
- new net VCC5: D53.A, Q34.3
- new net VCC_IN2: J14.72, J14.74, Q16.2, R39.2
- new net VCC_IN3: J19.72, J19.74, Q22.2, R56.2
- new net VCC_IN4: J24.72, J24.74, Q28.2, R73.2
- new net VCC_IN5: J29.72, J29.74, Q34.2, R90.2
- new net VIN2: C22.+, C23.+, C25.1, C27.1, D25.A, J13.70, J13.72, J13.74, R45.2, R46.2, R49.2, U6.1
- new net VIN3: C32.+, C33.+, C35.1, C37.1, D35.A, J18.70, J18.72, J18.74, R62.2, R63.2, R66.2, U8.1
- new net VIN4: C42.+, C43.+, C45.1, C47.1, D45.A, J23.70, J23.72, J23.74, R79.2, R80.2, R83.2, U10.1
- new net VIN5: C52.+, C53.+, C55.1, C57.1, D55.A, J28.70, J28.72, J28.74, R100.2, R96.2, R97.2, U12.1
- new net V_USB2: D21.5, D22.A, J11.VBUS1, J11.VBUS2, J13.13
- new net V_USB3: D31.5, D32.A, J16.VBUS1, J16.VBUS2, J18.13
- new net V_USB4: D41.5, D42.A, J21.VBUS1, J21.VBUS2, J23.13
- new net V_USB5: D51.5, D52.A, J26.VBUS1, J26.VBUS2, J28.13
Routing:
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- added copper zone on layer 1, net 3.3V2
- added copper zone on layer 1, net 3.3V3
- added copper zone on layer 1, net 3.3V4
- added copper zone on layer 1, net 3.3V5
- added copper zone on layer 1, net AUX1/DFU_!ACTIVE!/USR_BTN2
- added copper zone on layer 1, net AUX1/DFU_!ACTIVE!/USR_BTN3
- added copper zone on layer 1, net AUX1/DFU_!ACTIVE!/USR_BTN4
- added copper zone on layer 1, net AUX1/DFU_!ACTIVE!/USR_BTN5
- added copper zone on layer 1, net GND2
- added copper zone on layer 16, net GND2
- added copper zone on layer 1, net GND3
- added copper zone on layer 16, net GND3
- added copper zone on layer 1, net GND4
- added copper zone on layer 16, net GND4
- added copper zone on layer 1, net GND5
- added copper zone on layer 16, net GND5
- added copper zone on layer 1, net N$119
- added copper zone on layer 1, net N$56
- added copper zone on layer 1, net N$77
- added copper zone on layer 1, net N$98
- added copper zone on layer 1, net SHLD2
- added copper zone on layer 16, net SHLD2
- added copper zone on layer 1, net SHLD3
- added copper zone on layer 16, net SHLD3
- added copper zone on layer 1, net SHLD4
- added copper zone on layer 16, net SHLD4
- added copper zone on layer 1, net SHLD5
- added copper zone on layer 16, net SHLD5
- added copper zone on layer 1, net SIM_VCC2
- added copper zone on layer 16, net SIM_VCC2
- added copper zone on layer 1, net SIM_VCC3
- added copper zone on layer 16, net SIM_VCC3
- added copper zone on layer 1, net SIM_VCC4
- added copper zone on layer 16, net SIM_VCC4
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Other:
- board size 95.6 x 79.2 mm -> 133.6 x 149.6 mm
- board text added: "Do not remove"
- board text added: "v10"
- board text removed: "v02"
